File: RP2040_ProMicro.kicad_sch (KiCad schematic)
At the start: 52 parts, among them J1 HRO_TYPE-C-31-M-14, J2 Conn_01x16, J3 Battery, J4 Conn_01x18, J5 Conn_01x18, J6 Conn_01x12, Q1 SI2301A, SW1 SW_Push, U1 USBLC6-2SC6, U2 SOT23-5 200mA 3.3V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

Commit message: Routing in progress
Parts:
- removed C2, C6: 10uF, Capacitor_SMD:C_0402_1005Metric, symbol Device:C
- removed D1, D3: LED, LED_SMD:LED_1206_3216Metric, symbol Device:LED
- removed F1: 750 mA, Fuse:Fuse_0603_1608Metric, symbol Device:Fuse_Small
- removed J2: Conn_01x16, Connector_PinSocket_2.54mm:PinSocket_1x16_P2.54mm_Vertical, symbol Connector_Generic:Conn_01x16
- removed J3: Battery, Connector_JST:JST_EH_S2B-EH_1x02_P2.50mm_Horizontal, symbol Connector_Generic:Conn_01x02
- removed J6: Conn_01x12, Connector_PinSocket_2.54mm:PinSocket_1x12_P2.54mm_Vertical, symbol Connector_Generic:Conn_01x12
- removed L1: BLM15PX121SN1D, Inductor_SMD:L_0402_1005Metric, symbol Device:L_Small
- removed Q1: SI2301A, Package_TO_SOT_SMD:SOT-23, symbol Transistor_FET:AO3401A
- removed R11, R12, R7: 1k, Resistor_SMD:R_0402_1005Metric, symbol Device:R
- removed R3: 470, Resistor_SMD:R_0402_1005Metric, symbol Device:R
- removed R6: 2k, Resistor_SMD:R_0402_1005Metric, symbol Device:R
- removed SW1, SW?: SW_Push, Button_Switch_SMD:SW_Push_SPST_NO_Alps_SKRK, symbol Switch:SW_Push
- removed U3: TP4054, Package_TO_SOT_SMD:SOT-23-5, symbol Battery_Management:MCP73831-2-OT
- added J2: Conn_01x26, mikotofootprints:mikoto-pins, symbol Connector_Generic:Conn_01x26
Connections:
- net VBUS is gone; now on net +5V: J1.A4 (VBUS), J1.A9 (VBUS), J1.B4 (VBUS), J1.B9 (VBUS)
- net +3V3: no longer U4.26 (RUN)
- net +5V: now also C1.1, J2.1 (Pin_1), J2.22 (Pin_22), J2.25 (Pin_25), J2.26 (Pin_26); no longer C1.2
- net D+: now also U1.3 (I/O2); no longer U1.1 (I/O1)
- net D-: now also U1.1 (I/O1); no longer U1.3 (I/O2)
- net GND: now also C1.2, J2.24 (Pin_24), J2.4 (Pin_4), J2.5 (Pin_5); no longer C1.1
- net RESET: now also U4.26 (RUN), J2.23 (Pin_23)
- net USB_D+: now also U1.4 (I/O2); no longer U1.6 (I/O1)
- net USB_D-: now also U1.6 (I/O1); no longer U1.4 (I/O2)
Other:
- note removed: "Battery Charging"
- moved on the sheet: C10, C11, C12, C13, C14, C15, C16, C17, C18, C19, C20, D2

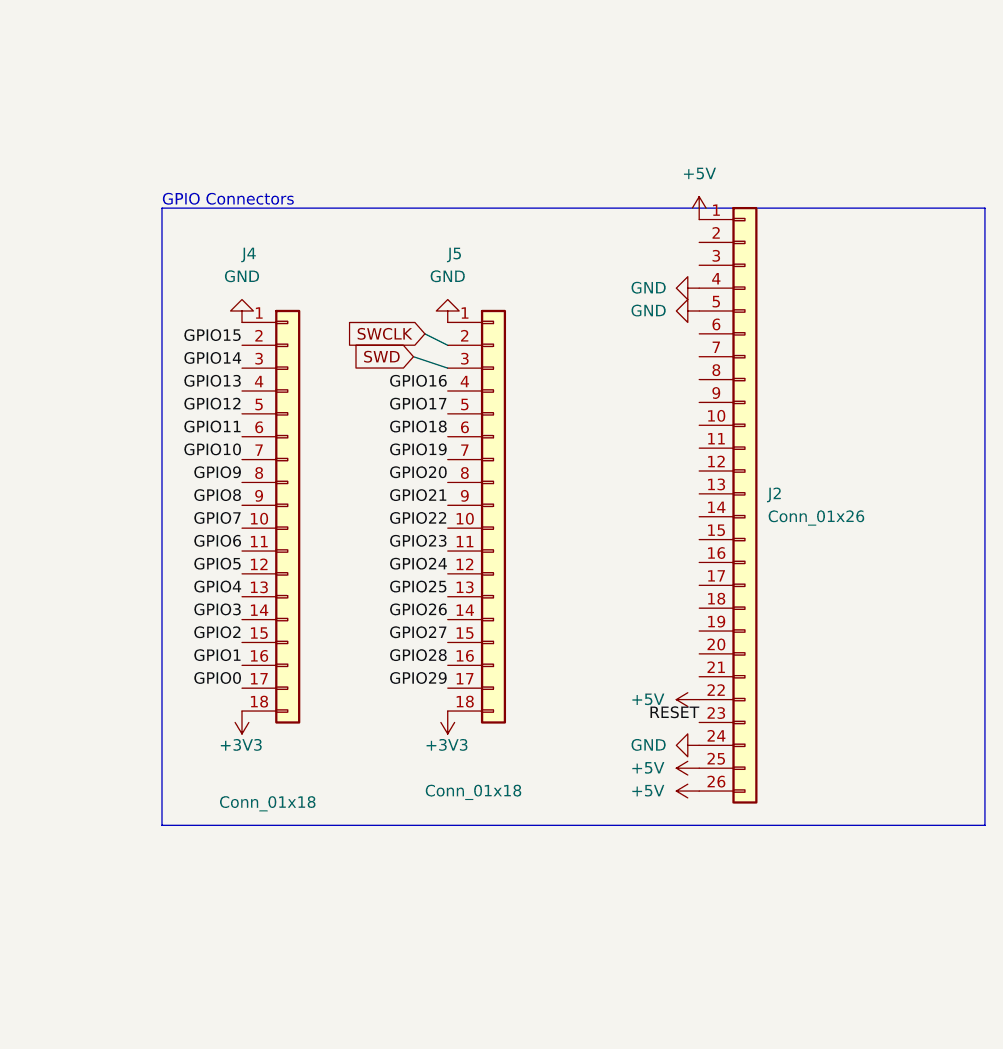
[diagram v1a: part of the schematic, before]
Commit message: added more vias around crystal
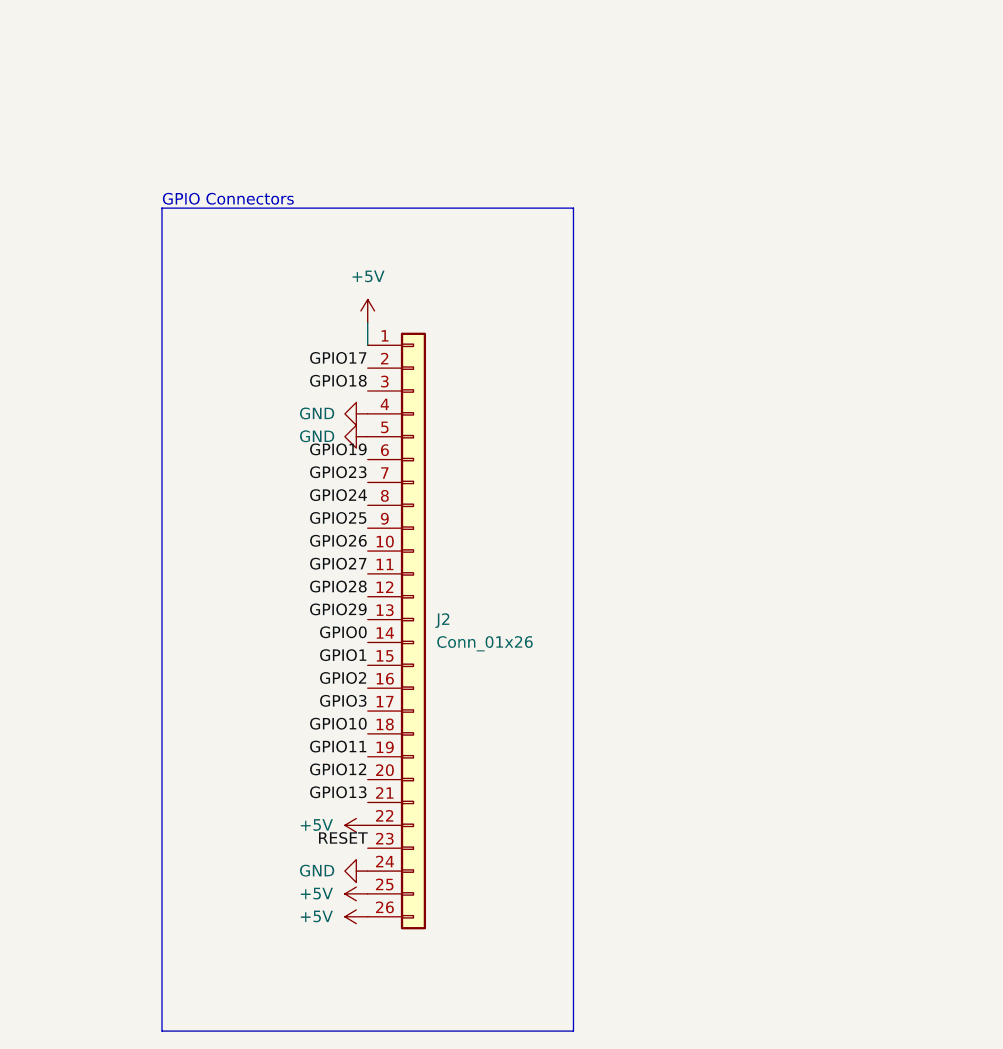
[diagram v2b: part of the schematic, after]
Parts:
- removed J4, J5: Conn_01x18, Connector_PinSocket_2.54mm:PinSocket_1x18_P2.54mm_Vertical, symbol Connector_Generic:Conn_01x18
- J2: footprint mikotofootprints:mikoto-pins -> mikotofootprints:promicrorp2040
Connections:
- net GPIO0: now also J2.14 (Pin_14)
- net GPIO1: now also J2.15 (Pin_15)
- net GPIO10: now also J2.18 (Pin_18)
- net GPIO11: now also J2.19 (Pin_19)
- net GPIO12: now also J2.20 (Pin_20)
- net GPIO13: now also J2.21 (Pin_21)
- net GPIO17: now also J2.2 (Pin_2)
- net GPIO18: now also J2.3 (Pin_3)
- net GPIO19: now also J2.6 (Pin_6)
- net GPIO2: now also J2.16 (Pin_16)
- net GPIO23: now also J2.7 (Pin_7)
- net GPIO24: now also J2.8 (Pin_8)
- net GPIO25: now also J2.9 (Pin_9)
- net GPIO26: now also J2.10 (Pin_10)
- net GPIO27: now also J2.11 (Pin_11)
- net GPIO28: now also J2.12 (Pin_12)
- net GPIO29: now also J2.13 (Pin_13)
- net GPIO3: now also J2.17 (Pin_17)
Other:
- moved on the sheet: J2
